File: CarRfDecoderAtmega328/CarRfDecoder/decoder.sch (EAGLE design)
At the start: 45 parts, among them T1 BC847, T2 BC847, T3 IRLML6402, U2 RFM69CW, U3 MCP73831, U4 ATMEGA328P, U6 MIC5219 3.3V

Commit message: changes in the design
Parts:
- added C1, C5: 22pF, SparkFun-Capacitors:CAP0805
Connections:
- new net N$2: C1.2, U4.PB6(XTAL1/TOSC1)
- new net N$4: C5.2, U4.PB7(XTAL2/TOSC2)
- net GND: now also C1.1, C5.1
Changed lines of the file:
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@@
 <part name="SCK" library="wirepad" deviceset="SMD2" device=""/>
 <part name="SERIAL_DTR" library="wirepad" deviceset="SMD2" device=""/>
+<part name="C1" library="SparkFun-Capacitors" deviceset="CAP" device="0805" value="22pF"/>
+<part name="C5" library="SparkFun-Capacitors" deviceset="CAP" device="0805" value="22pF"/>
 </parts>
 <sheets>
@@
 <instance part="SCK" gate="1" x="119.38" y="12.7" rot="MR0"/>
 <instance part="SERIAL_DTR" gate="1" x="-35.56" y="101.6"/>
+<instance part="C1" gate="G$1" x="10.16" y="48.26" rot="R90"/>
+<instance part="C5" gate="G$1" x="10.16" y="43.18" rot="R90"/>
 </instances>
 <busses>
@@
 <pinref part="GND3" gate="1" pin="GND"/>
 <junction x="27.94" y="17.78"/>
+<pinref part="C5" gate="G$1" pin="1"/>
+<wire x1="5.08" y1="43.18" x2="2.54" y2="43.18" width="0.1524" layer="91"/>
+<wire x1="2.54" y1="43.18" x2="2.54" y2="45.72" width="0.1524" layer="91"/>
+<pinref part="C1" gate="G$1" pin="1"/>
+<wire x1="2.54" y1="45.72" x2="2.54" y2="48.26" width="0.1524" layer="91"/>
+<wire x1="2.54" y1="48.26" x2="5.08" y2="48.26" width="0.1524" layer="91"/>
+<wire x1="2.54" y1="45.72" x2="-2.54" y2="45.72" width="0.1524" layer="91"/>
+<wire x1="-2.54" y1="45.72" x2="-2.54" y2="17.78" width="0.1524" layer="91"/>
+<junction x="2.54" y="45.72"/>
+<wire x1="-2.54" y1="17.78" x2="27.94" y2="17.78" width="0.1524" layer="91"/>
 </segment>
 </net>
@@
 </segment>
 </net>
+<net name="N$2" class="0">
+<segment>
+<pinref part="C1" gate="G$1" pin="2"/>
+<pinref part="U4" gate="G$1" pin="PB6(XTAL1/TOSC1)"/>
+<wire x1="12.7" y1="48.26" x2="30.48" y2="48.26" width="0.1524" layer="91"/>
+</segment>
+</net>
+<net name="N$4" class="0">
+<segment>
+<pinref part="C5" gate="G$1" pin="2"/>
+<pinref part="U4" gate="G$1" pin="PB7(XTAL2/TOSC2)"/>
+<wire x1="12.7" y1="43.18" x2="30.48" y2="43.18" width="0.1524" layer="91"/>
+</segment>
+</net>

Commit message: some improvement on the boards.
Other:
- moved on the sheet: BAT+, BATGND, SERIAL_DTR, SERIAL_GND, SERIAL_RX, SERIAL_TX, SERIAL_V+
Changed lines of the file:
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@@
 </plain>
 <instances>
-<instance part="SERIAL_V+" gate="1" x="-35.56" y="116.84"/>
-<instance part="SERIAL_TX" gate="1" x="-35.56" y="111.76"/>
-<instance part="SERIAL_RX" gate="1" x="-35.56" y="106.68"/>
-<instance part="BATGND" gate="1" x="-35.56" y="127"/>
-<instance part="BAT+" gate="1" x="-35.56" y="132.08"/>
-<instance part="GND4" gate="1" x="-15.24" y="121.92"/>
+<instance part="SERIAL_V+" gate="1" x="-17.78" y="116.84"/>
+<instance part="SERIAL_TX" gate="1" x="-17.78" y="111.76"/>
+<instance part="SERIAL_RX" gate="1" x="-17.78" y="106.68"/>
+<instance part="BATGND" gate="1" x="-17.78" y="127"/>
+<instance part="BAT+" gate="1" x="-17.78" y="132.08"/>
+<instance part="GND4" gate="1" x="2.54" y="121.92"/>
 <instance part="U3" gate="G$1" x="25.4" y="114.3"/>
 <instance part="GND5" gate="1" x="38.1" y="106.68"/>
@@
 <instance part="GND3" gate="1" x="27.94" y="15.24"/>
 <instance part="VCC3" gate="G$1" x="25.4" y="66.04"/>
-<instance part="SERIAL_GND" gate="1" x="-35.56" y="121.92"/>
+<instance part="SERIAL_GND" gate="1" x="-17.78" y="121.92"/>
 <instance part="R1" gate="G$1" x="15.24" y="73.66"/>
 <instance part="VCC4" gate="G$1" x="2.54" y="73.66"/>
@@
 <instance part="SO" gate="1" x="119.38" y="17.78" rot="MR0"/>
 <instance part="SCK" gate="1" x="119.38" y="12.7" rot="MR0"/>
-<instance part="SERIAL_DTR" gate="1" x="-35.56" y="101.6"/>
+<instance part="SERIAL_DTR" gate="1" x="-17.78" y="101.6"/>
 <instance part="C1" gate="G$1" x="10.16" y="48.26" rot="R90"/>
 <instance part="C5" gate="G$1" x="10.16" y="43.18" rot="R90"/>
@@
 <segment>
 <pinref part="BATGND" gate="1" pin="P"/>
-<wire x1="-33.02" y1="127" x2="-20.32" y2="127" width="0.1524" layer="91"/>
-<wire x1="-20.32" y1="127" x2="-15.24" y2="127" width="0.1524" layer="91"/>
-<wire x1="-15.24" y1="127" x2="-15.24" y2="124.46" width="0.1524" layer="91"/>
+<wire x1="-15.24" y1="127" x2="-2.54" y2="127" width="0.1524" layer="91"/>
+<wire x1="-2.54" y1="127" x2="2.54" y2="127" width="0.1524" layer="91"/>
+<wire x1="2.54" y1="127" x2="2.54" y2="124.46" width="0.1524" layer="91"/>
 <pinref part="GND4" gate="1" pin="GND"/>
 <pinref part="SERIAL_GND" gate="1" pin="P"/>
-<wire x1="-33.02" y1="121.92" x2="-20.32" y2="121.92" width="0.1524" layer="91"/>
-<wire x1="-20.32" y1="121.92" x2="-20.32" y2="127" width="0.1524" layer="91"/>
-<junction x="-20.32" y="127"/>
+<wire x1="-15.24" y1="121.92" x2="-2.54" y2="121.92" width="0.1524" layer="91"/>
+<wire x1="-2.54" y1="121.92" x2="-2.54" y2="127" width="0.1524" layer="91"/>
+<junction x="-2.54" y="127"/>
 </segment>
 <segment>
@@
 <pinref part="U3" gate="G$1" pin="VIN"/>
 <pinref part="SERIAL_V+" gate="1" pin="P"/>
-<wire x1="15.24" y1="116.84" x2="-33.02" y2="116.84" width="0.1524" layer="91"/>
+<wire x1="15.24" y1="116.84" x2="-15.24" y2="116.84" width="0.1524" layer="91"/>
 </segment>
 </net>
@@
 <wire x1="66.04" y1="119.38" x2="71.12" y2="119.38" width="0.1524" layer="91"/>
 <pinref part="BAT+" gate="1" pin="P"/>
-<wire x1="-33.02" y1="132.08" x2="40.64" y2="132.08" width="0.1524" layer="91"/>
+<wire x1="-15.24" y1="132.08" x2="40.64" y2="132.08" width="0.1524" layer="91"/>
 <junction x="40.64" y="132.08"/>
 <wire x1="40.64" y1="132.08" x2="58.42" y2="132.08" width="0.1524" layer="91"/>
@@
 <segment>
 <pinref part="SERIAL_TX" gate="1" pin="P"/>
-<wire x1="-33.02" y1="111.76" x2="-27.94" y2="111.76" width="0.1524" layer="91"/>
-<label x="-20.32" y="111.76" size="1.778" layer="95"/>
+<wire x1="-15.24" y1="111.76" x2="-10.16" y2="111.76" width="0.1524" layer="91"/>
+<label x="-2.54" y="111.76" size="1.778" layer="95"/>
 </segment>
 </net>
@@
 <segment>
 <pinref part="SERIAL_RX" gate="1" pin="P"/>
-<wire x1="-33.02" y1="106.68" x2="-27.94" y2="106.68" width="0.1524" layer="91"/>
-<label x="-20.32" y="106.68" size="1.778" layer="95"/>
+<wire x1="-15.24" y1="106.68" x2="-10.16" y2="106.68" width="0.1524" layer="91"/>
+<label x="-2.54" y="106.68" size="1.778" layer="95"/>
 </segment>
 </net>
@@
 <pinref part="SERIAL_DTR" gate="1" pin="P"/>
 <wire x1="25.4" y1="73.66" x2="30.48" y2="73.66" width="0.1524" layer="91"/>
-<wire x1="-33.02" y1="101.6" x2="25.4" y2="101.6" width="0.1524" layer="91"/>
+<wire x1="-15.24" y1="101.6" x2="25.4" y2="101.6" width="0.1524" layer="91"/>
 <wire x1="25.4" y1="101.6" x2="25.4" y2="73.66" width="0.1524" layer="91"/>
 <junction x="25.4" y="73.66"/>

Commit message: Ready boards.
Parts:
- added VJ, VJ1, XTAL, XTAL1: (no value), wirepad:SMD2
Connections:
- new net N$1: U2.3.3V, VJ.P
- net N$2: now also XTAL.P
- net N$4: now also XTAL1.P
- net VCC: now also VJ1.P; no longer U2.3.3V
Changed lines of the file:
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@@
 <part name="C1" library="SparkFun-Capacitors" deviceset="CAP" device="0805" value="22pF"/>
 <part name="C5" library="SparkFun-Capacitors" deviceset="CAP" device="0805" value="22pF"/>
+<part name="XTAL" library="wirepad" deviceset="SMD2" device=""/>
+<part name="XTAL1" library="wirepad" deviceset="SMD2" device=""/>
+<part name="VJ" library="wirepad" deviceset="SMD2" device=""/>
+<part name="VJ1" library="wirepad" deviceset="SMD2" device=""/>
 </parts>
 <sheets>
@@
 <instance part="U2" gate="G$1" x="50.8" y="-25.4"/>
 <instance part="GND12" gate="1" x="71.12" y="-40.64"/>
-<instance part="SUPPLY1" gate="G$1" x="27.94" y="-10.16"/>
+<instance part="SUPPLY1" gate="G$1" x="33.02" y="-5.08"/>
 <instance part="U4" gate="G$1" x="53.34" y="48.26"/>
 <instance part="GND3" gate="1" x="27.94" y="15.24"/>
@@
 <instance part="C1" gate="G$1" x="10.16" y="48.26" rot="R90"/>
 <instance part="C5" gate="G$1" x="10.16" y="43.18" rot="R90"/>
+<instance part="XTAL" gate="1" x="22.86" y="53.34" rot="MR0"/>
+<instance part="XTAL1" gate="1" x="22.86" y="38.1" rot="MR0"/>
+<instance part="VJ" gate="1" x="27.94" y="-12.7" rot="MR180"/>
+<instance part="VJ1" gate="1" x="27.94" y="-5.08" rot="MR180"/>
 </instances>
 <busses>
@@
 </segment>
 <segment>
-<pinref part="U2" gate="G$1" pin="3.3V"/>
-<wire x1="35.56" y1="-15.24" x2="27.94" y2="-15.24" width="0.1524" layer="91"/>
-<wire x1="27.94" y1="-15.24" x2="27.94" y2="-10.16" width="0.1524" layer="91"/>
+<pinref part="VJ1" gate="1" pin="P"/>
 <pinref part="SUPPLY1" gate="G$1" pin="VCC"/>
+<wire x1="33.02" y1="-5.08" x2="30.48" y2="-5.08" width="0.1524" layer="91"/>
 </segment>
 <segment>
@@
 <pinref part="C1" gate="G$1" pin="2"/>
 <pinref part="U4" gate="G$1" pin="PB6(XTAL1/TOSC1)"/>
-<wire x1="12.7" y1="48.26" x2="30.48" y2="48.26" width="0.1524" layer="91"/>
+<wire x1="12.7" y1="48.26" x2="20.32" y2="48.26" width="0.1524" layer="91"/>
+<pinref part="XTAL" gate="1" pin="P"/>
+<wire x1="20.32" y1="48.26" x2="30.48" y2="48.26" width="0.1524" layer="91"/>
+<wire x1="20.32" y1="53.34" x2="20.32" y2="48.26" width="0.1524" layer="91"/>
+<junction x="20.32" y="48.26"/>
 </segment>
 </net>
@@
 <pinref part="C5" gate="G$1" pin="2"/>
 <pinref part="U4" gate="G$1" pin="PB7(XTAL2/TOSC2)"/>
-<wire x1="12.7" y1="43.18" x2="30.48" y2="43.18" width="0.1524" layer="91"/>
-</segment>
-</net>
+<wire x1="12.7" y1="43.18" x2="20.32" y2="43.18" width="0.1524" layer="91"/>
+<pinref part="XTAL1" gate="1" pin="P"/>
+<wire x1="20.32" y1="43.18" x2="30.48" y2="43.18" width="0.1524" layer="91"/>
+<wire x1="20.32" y1="38.1" x2="20.32" y2="43.18" width="0.1524" layer="91"/>
+<junction x="20.32" y="43.18"/>
+</segment>
+</net>
+<net name="N$1" class="0">
+<segment>
+<pinref part="U2" gate="G$1" pin="3.3V"/>
+<pinref part="VJ" gate="1" pin="P"/>
+<wire x1="35.56" y1="-15.24" x2="30.48" y2="-12.7" width="0.1524" layer="91"/>
+</segment>
+</net>

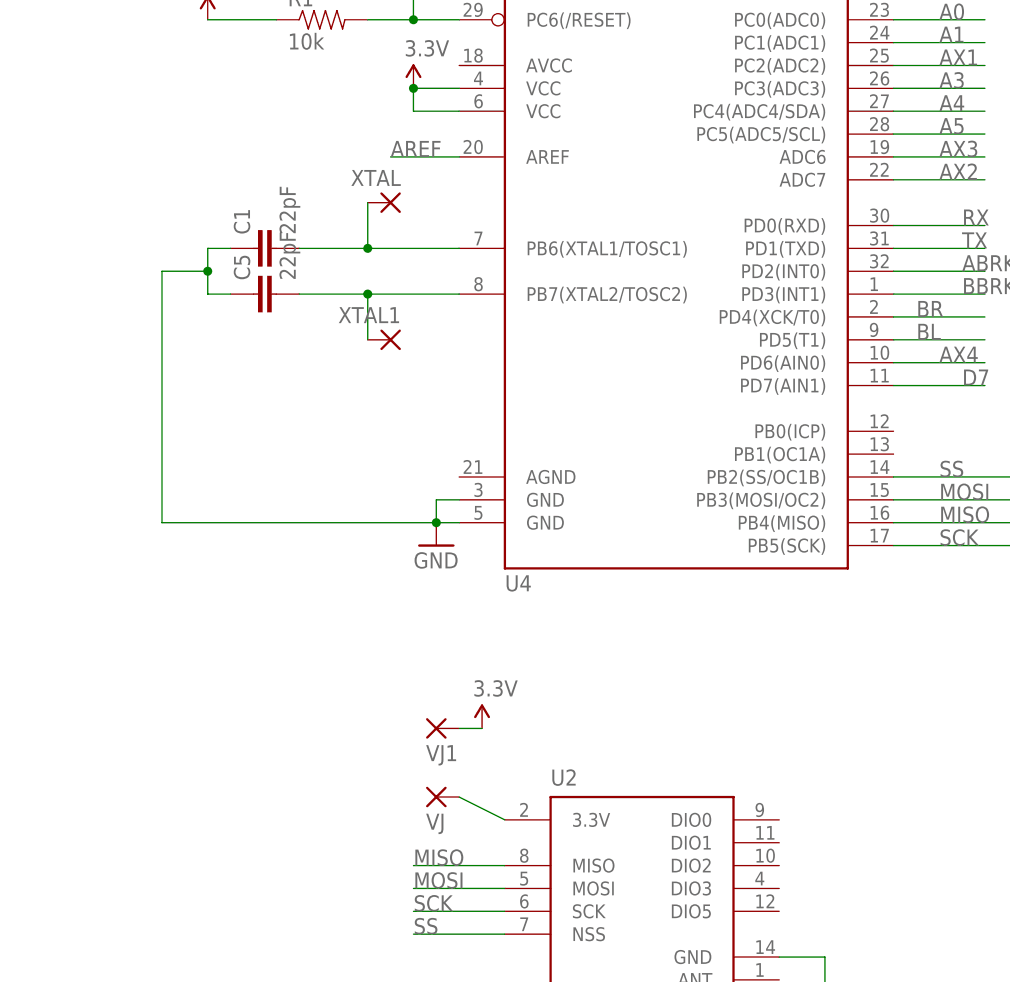
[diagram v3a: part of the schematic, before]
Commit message: Fix connection to the rf module and add a 16mhz crystal
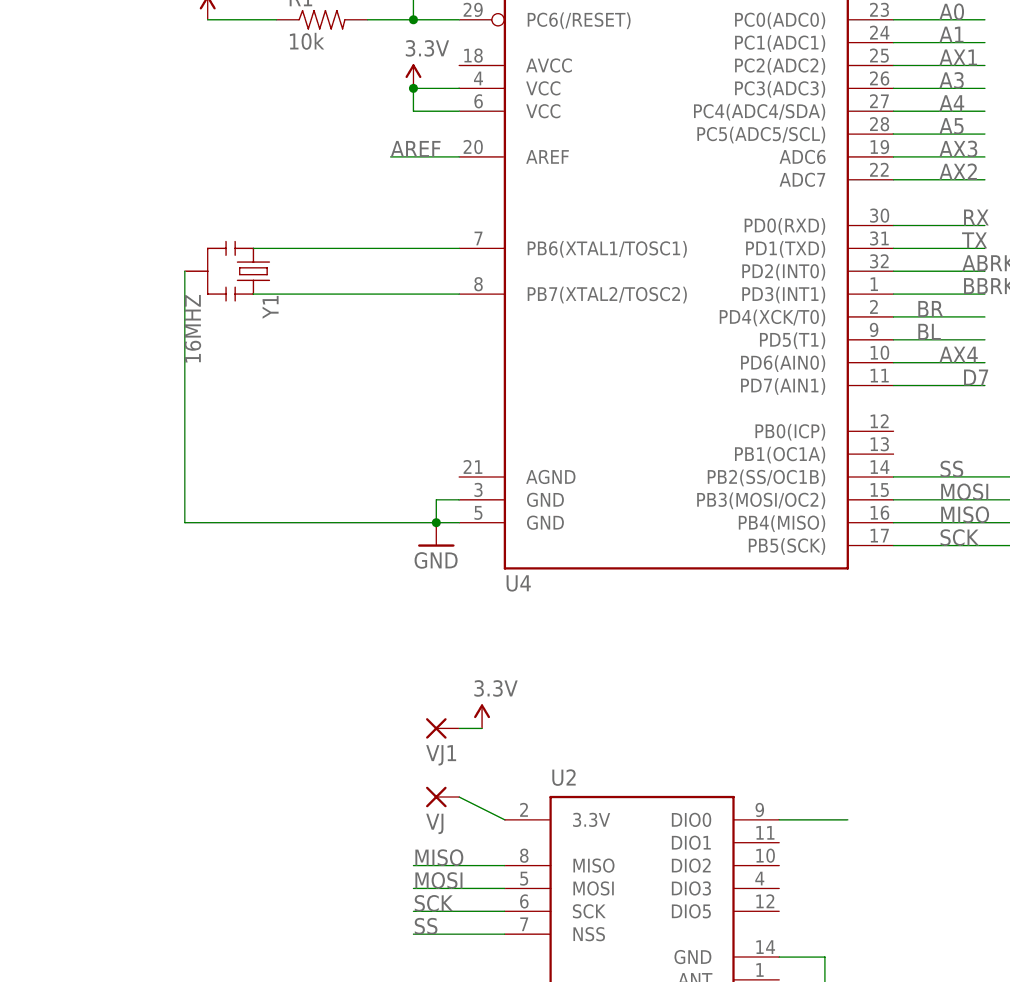
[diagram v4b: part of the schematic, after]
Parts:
- removed C1, C5: 22pF, SparkFun-Capacitors:CAP0805
- removed XTAL, XTAL1: (no value), wirepad:SMD2
- added Y1: 16MHZ, SparkFun-FreqCtrl:RESONATOR16MHZ
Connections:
- net ABRKL: now also U2.DIO0
- net GND: now also Y1.2; no longer C1.1, C5.1
- net N$2: now also Y1.1; no longer C1.2, XTAL.P
- net N$4: now also Y1.3; no longer C5.2, XTAL1.P
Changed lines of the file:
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@@
 <part name="SCK" library="wirepad" deviceset="SMD2" device=""/>
 <part name="SERIAL_DTR" library="wirepad" deviceset="SMD2" device=""/>
-<part name="C1" library="SparkFun-Capacitors" deviceset="CAP" device="0805" value="22pF"/>
-<part name="C5" library="SparkFun-Capacitors" deviceset="CAP" device="0805" value="22pF"/>
-<part name="XTAL" library="wirepad" deviceset="SMD2" device=""/>
-<part name="XTAL1" library="wirepad" deviceset="SMD2" device=""/>
 <part name="VJ" library="wirepad" deviceset="SMD2" device=""/>
 <part name="VJ1" library="wirepad" deviceset="SMD2" device=""/>
+<part name="Y1" library="SparkFun-FreqCtrl" deviceset="RESONATOR" device="16MHZ" value="16MHZ"/>
 </parts>
 <sheets>
@@
 <instance part="SCK" gate="1" x="119.38" y="12.7" rot="MR0"/>
 <instance part="SERIAL_DTR" gate="1" x="-17.78" y="101.6"/>
-<instance part="C1" gate="G$1" x="10.16" y="48.26" rot="R90"/>
-<instance part="C5" gate="G$1" x="10.16" y="43.18" rot="R90"/>
-<instance part="XTAL" gate="1" x="22.86" y="53.34" rot="MR0"/>
-<instance part="XTAL1" gate="1" x="22.86" y="38.1" rot="MR0"/>
 <instance part="VJ" gate="1" x="27.94" y="-12.7" rot="MR180"/>
 <instance part="VJ1" gate="1" x="27.94" y="-5.08" rot="MR180"/>
+<instance part="Y1" gate="G$1" x="7.62" y="45.72" rot="R270"/>
 </instances>
 <busses>
@@
 <pinref part="GND3" gate="1" pin="GND"/>
 <junction x="27.94" y="17.78"/>
-<pinref part="C5" gate="G$1" pin="1"/>
-<wire x1="5.08" y1="43.18" x2="2.54" y2="43.18" width="0.1524" layer="91"/>
-<wire x1="2.54" y1="43.18" x2="2.54" y2="45.72" width="0.1524" layer="91"/>
-<pinref part="C1" gate="G$1" pin="1"/>
-<wire x1="2.54" y1="45.72" x2="2.54" y2="48.26" width="0.1524" layer="91"/>
-<wire x1="2.54" y1="48.26" x2="5.08" y2="48.26" width="0.1524" layer="91"/>
-<wire x1="2.54" y1="45.72" x2="-2.54" y2="45.72" width="0.1524" layer="91"/>
-<wire x1="-2.54" y1="45.72" x2="-2.54" y2="17.78" width="0.1524" layer="91"/>
-<junction x="2.54" y="45.72"/>
-<wire x1="-2.54" y1="17.78" x2="27.94" y2="17.78" width="0.1524" layer="91"/>
+<pinref part="Y1" gate="G$1" pin="2"/>
+<wire x1="0" y1="17.78" x2="27.94" y2="17.78" width="0.1524" layer="91"/>
+<wire x1="0" y1="45.72" x2="0" y2="17.78" width="0.1524" layer="91"/>
 </segment>
 </net>
@@
 <label x="86.36" y="45.72" size="1.778" layer="95"/>
 </segment>
+<segment>
+<pinref part="U2" gate="G$1" pin="DIO0"/>
+<wire x1="66.04" y1="-15.24" x2="73.66" y2="-15.24" width="0.1524" layer="91"/>
+</segment>
 </net>
 <net name="AX1" class="0">
@@
 <net name="N$2" class="0">
 <segment>
-<pinref part="C1" gate="G$1" pin="2"/>
 <pinref part="U4" gate="G$1" pin="PB6(XTAL1/TOSC1)"/>
-<wire x1="12.7" y1="48.26" x2="20.32" y2="48.26" width="0.1524" layer="91"/>
-<pinref part="XTAL" gate="1" pin="P"/>
-<wire x1="20.32" y1="48.26" x2="30.48" y2="48.26" width="0.1524" layer="91"/>
-<wire x1="20.32" y1="53.34" x2="20.32" y2="48.26" width="0.1524" layer="91"/>
-<junction x="20.32" y="48.26"/>
+<wire x1="7.62" y1="48.26" x2="30.48" y2="48.26" width="0.1524" layer="91"/>
+<pinref part="Y1" gate="G$1" pin="1"/>
 </segment>
 </net>
 <net name="N$4" class="0">
 <segment>
-<pinref part="C5" gate="G$1" pin="2"/>
 <pinref part="U4" gate="G$1" pin="PB7(XTAL2/TOSC2)"/>
-<wire x1="12.7" y1="43.18" x2="20.32" y2="43.18" width="0.1524" layer="91"/>
-<pinref part="XTAL1" gate="1" pin="P"/>
-<wire x1="20.32" y1="43.18" x2="30.48" y2="43.18" width="0.1524" layer="91"/>
-<wire x1="20.32" y1="38.1" x2="20.32" y2="43.18" width="0.1524" layer="91"/>
-<junction x="20.32" y="43.18"/>
-</segment>
-</net>
+<wire x1="7.62" y1="43.18" x2="30.48" y2="43.18" width="0.1524" layer="91"/>
+<pinref part="Y1" gate="G$1" pin="3"/>
+</segment>
+</net>
